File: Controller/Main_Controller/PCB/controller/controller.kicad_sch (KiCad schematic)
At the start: 118 parts, among them Q1 S9013, U1 NUCLEO144-F429ZI, U2 Joystick, U3 Joystick, U4 ZSR330GTA, U5 ZLDO1117G50TA

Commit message: Add Reverse polarity protection
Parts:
- removed D4, D5: B5817W-5819W, Diode_SMD:D_SOD-123, symbol Diode:1N5817
- added D?: D, symbol Device:D
- added Q?: Q_PMOS_DGS, symbol Device:Q_PMOS_DGS
- added R?: R, symbol Device:R
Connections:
- net Earth: now also R?.2
- net VIN: now also Q?.1 (D); no longer PWR_SW1.2 (B)
- new net: D?.2 (A), Q?.2 (G), R?.1
- new net: D?.1 (K), PWR_SW1.2 (B), Q?.3 (S)
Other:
- moved on the sheet: C?, D?, M?, PWR_SW1, Q?, R?, U1

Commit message: uPDATE sCHEMATIC - ADD MOST BUTTONS
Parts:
- removed BTN, D_SEL, RESET?: SW_SPST, Button_Switch_SMD:SW_Push_1P1T_NO_6x6mm_H9.5mm, symbol Switch:SW_SPST
- removed C? (x7): 100nF, Capacitor_SMD:C_0603_1608Metric, symbol Device:C
- removed D? (x7): D, symbol Device:D
- removed R? (x14): 47K, Resistor_SMD:R_0603_1608Metric, symbol Device:R
- removed R?: 2K2, Resistor_SMD:R_0603_1608Metric, symbol Device:R
- removed R?: 10K, Resistor_SMD:R_0603_1608Metric, symbol Device:R
- removed U? (x14): 74HC7014, Package_SO:SOIC-14_3.9x8.7mm_P1.27mm, symbol 74xx:74HC7014
- added ASCEND, DESCEND, LIGHTS, MOTOR_ENGAGE, REV_BRAKE, REV_BRAKE?: SW_SPDT, symbol Switch:SW_SPDT
- added C? (x16): 100nF, Capacitor_SMD:C_0603_1608Metric, symbol Device:C
- added D? (x16): D, symbol Device:D
- added D_BACK, D_SELECT, KILL_SWITCH: SW_SPST, Button_Switch_SMD:SW_Push_1P1T_NO_6x6mm_H9.5mm, symbol Switch:SW_SPST
- added J?: Conn_01x10, symbol Connector_Generic:Conn_01x10
- added R? (x32): 47K, Resistor_SMD:R_0603_1608Metric, symbol Device:R
- added R? (x2): 4K7, Resistor_SMD:R_0603_1608Metric, symbol Device:R
- added U? (x21): 74HC7014, Package_SO:SOIC-14_3.9x8.7mm_P1.27mm, symbol 74xx:74HC7014
- gave numbers to parts that had none: 1
- renumbered R2 to R?, R1 to R?, RESET1 to RESET
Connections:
- net RESET_1 is gone; now on net RESET: A1.3 (~{RESET}), R3.2
- net +3V3: now also U1.16 (+3V3), R?.1, R?.1, U?.14 (VCC), U?.14 (VCC), U?.14 (VCC)
- net +5V: now also U1.18 (+5V), R?.2, R?.2, R?.2, R?.2, R?.2, R?.2, R?.2, R?.2, R?.2, R?.2, R?.2, R?.2, R?.2, R?.2, R?.2, R?.2
- net D_DOWN: now also A1.20 (A1), U?.4
- net D_LEFT: now also A1.21 (A2), U?.6
- net D_RIGHT: now also A1.22 (A3), U?.8
- net D_UP: now also A1.19 (A0), U?.2
- net Earth: now also U1.111 (GND), U1.126 (GND), U1.135 (GND), U1.143 (GND), U1.144 (GND), U1.19 (GND), U1.20 (GND), U1.22 (GND), U1.49 (GND), U1.60 (GND), U1.71 (GND), U1.72 (GND), U1.8 (GND), U1.81 (GND), U1.92 (GND), ASCEND.2 (B), C?.1, C?.1, C?.1, C?.1, C?.1, C?.1, C?.1, C?.1, C?.1, C?.1, C?.1, C?.1, C?.1, C?.1, C?.1, C?.1, DESCEND.2 (B), D_BACK.1 (A), D_SELECT.1 (A), J?.2 (Pin_2), J?.5 (Pin_5), J?.8 (Pin_8), KILL_SWITCH.1 (A), LIGHTS.2 (B), MOTOR_ENGAGE.2 (B), REV_BRAKE.2 (B), REV_BRAKE?.2 (B), U?.7 (GND), U?.7 (GND), U?.7 (GND)
- net LCD_E: now also A1.6 (D3); no longer A1.10 (D7)
- net LCD_R/W: now also A1.9 (D6); no longer A1.11 (D8)
- net LED_1: now also A1.5 (D2); no longer A1.2 (D0/RX)
- net MOTOR_MODE_1: now also U?.2
- net MOTOR_MODE_2: now also U?.4
- net VIN: now also J?.1 (Pin_1)
- net D_SELECT: now reaches A1.25 (A6)
- net D_SELECT: now also U?.10
- net D_BACK: now reaches A1.26 (A7)
- net D_BACK: now also U?.12
- net SDA_1: now reaches A1.7 (D4)
- net SDA_1: now also J?.3 (Pin_3), R?.2
- net CLK_1: now reaches A1.8 (D5)
- net CLK_1: now also R?.2
- net at MOTOR_MODE.3 (C): now also D?.2 (A), R?.1, R?.2
- net at D_RIGHT.2 (B): now also D?.2 (A), R?.1, R?.2
- net at MOTOR_MODE.1 (A): now also D?.2 (A), R?.1, R?.2
- net at D_LEFT.2 (B): now also D?.2 (A), R?.1, R?.2
- net RESET: now reaches U1.14 (~{RST})
- net at C?.2, D?.1 (K), R?.1: now also U?.1
- net at D_DOWN.2 (B): now also D?.2 (A), R?.1, R?.2
- new net: C?.2, D?.1 (K), R?.1, U?.13 (x2)
- new net: D?.2 (A), MOTOR_ENGAGE.1 (A), R?.1, R?.2
- new net: C?.2, D?.1 (K), R?.1, U?.3 (x3)
- new net: C?.2, D?.1 (K), R?.1, U?.5 (x3)
- new net: D?.2 (A), R?.1, R?.2, REV_BRAKE?.1 (A)
- new net: C?.2, D?.1 (K), R?.1, U?.1 (x2)
- new net: D?.2 (A), R?.1, R?.2, REV_BRAKE?.3 (C)
- new net: C?.2, D?.1 (K), R?.1, U?.9 (x3)
- new net: D?.2 (A), D_BACK.2 (B), R?.1, R?.2
- new net: D?.2 (A), R?.1, R?.2, REV_BRAKE.3 (C)
- new net: D?.2 (A), R?.1, R?.2, REV_BRAKE.1 (A)
- new net: D?.2 (A), KILL_SWITCH.2 (B), R?.1, R?.2
- new net: C?.2, D?.1 (K), R?.1
- new net: ASCEND.1 (A), D?.2 (A), R?.1, R?.2
- new net: C?.2, D?.1 (K), R?.1, U?.11 (x2)
- new net: D?.2 (A), DESCEND.1 (A), R?.1, R?.2
- new net: D?.2 (A), D_SELECT.2 (B), R?.1, R?.2
- new net: D?.2 (A), LIGHTS.1 (A), R?.1, R?.2
- new net ASCEND: U?.8
- new net BRAKE_MODE: U?.2
- new net DESCEND: U?.10
- new net DET_IN: J?.9 (Pin_9)
- new net DET_OUT: J?.10 (Pin_10)
- new net KILL_SWITCH: U?.6
- new net MOTOR_DENGAGE: U?.8
- new net MOTOR_ENGAGE: U?.12, U?.6
- new net REV_MODE: U?.4
- new net SCK_1: J?.4 (Pin_4)
- new net SCK_2: J?.7 (Pin_7)
- new net SDA_2: J?.6 (Pin_6)
- no-connect marks 12 -> 31
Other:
- note added: "BUZZER"
- note added: "CONNECTOR"
- note added: "D-PAD"
- note added: "JOYSTICKS"
- note added: "LCD"
- note added: "NUCLEO-F429ZI"
- note added: "NUCLEO-L432KC"
- note added: "POWER"
- note added: "VIBRATION MOTOR"
- company: Luke W -> Sirmon Industries, Luke Waller, Noah Harvey, Jack Pendlebury, Daniel Cole 
- title: Project ORCA Controller -> HEVCS Controller
- moved on the sheet: A1, BZ?, C1, C2, C3, C4, C?, D1, D2, D3, D?, DS?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

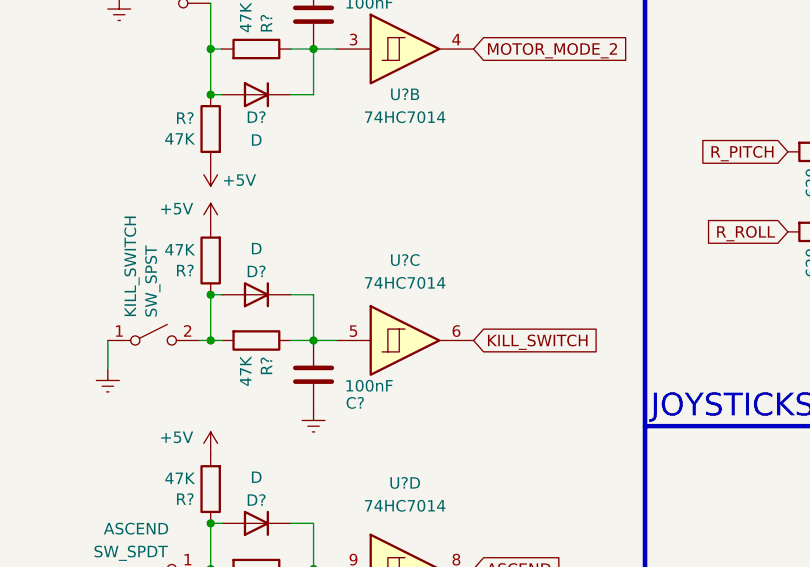
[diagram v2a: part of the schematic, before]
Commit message: verified schmitt trigger functionality
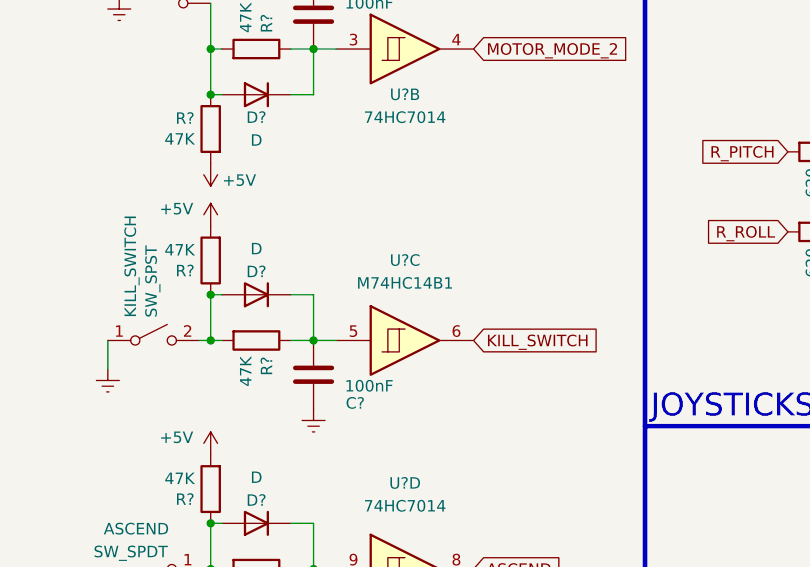
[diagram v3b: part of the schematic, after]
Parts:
- U?: value 74HC7014 -> M74HC14B1
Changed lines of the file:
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@@
     (in_bom yes) (on_board yes) (fields_autoplaced)
     (property "Reference" "U?" (id 0) (at 233.68 68.58 0))
-    (property "Value" "74HC7014" (id 1) (at 233.68 71.12 0))
+    (property "Value" "M74HC14B1" (id 1) (at 233.68 71.12 0))
     (property "Footprint" "Package_SO:SOIC-14_3.9x8.7mm_P1.27mm" (id 2) (at 233.68 77.47 0)
       (effects (font (size 1.27 1.27)) hide)
@@
     )
     (path "/afe26da9-bfe2-4ef8-993f-8605163ec6eb"
-      (reference "U?") (unit 3) (value "74HC7014") (footprint "Package_SO:SOIC-14_3.9x8.7mm_P1.27mm")
+      (reference "U?") (unit 3) (value "M74HC14B1") (footprint "Package_SO:SOIC-14_3.9x8.7mm_P1.27mm")
     )
     (path "/e7f76d38-76ff-4182-add0-0aac4e530149"

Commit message: started adding solder bridges
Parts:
- removed C?: 100nF, Capacitor_SMD:C_0603_1608Metric, symbol Device:C
- removed D?: D, symbol Device:D
- removed MOTOR_ENGAGE: SW_SPDT, symbol Switch:SW_SPDT
- removed R? (x2): 47K, Resistor_SMD:R_0603_1608Metric, symbol Device:R
- removed U?: 74HC7014, Package_SO:SOIC-14_3.9x8.7mm_P1.27mm, symbol 74xx:74HC7014
- added C? (x3): 100nF, Capacitor_SMD:C_0603_1608Metric, symbol Device:C
- added JP? (x7): SolderJumper_3_Open, symbol Jumper:SolderJumper_3_Open
- added U?: 74HC7014, Package_SO:SOIC-14_3.9x8.7mm_P1.27mm, symbol 74xx:74HC7014
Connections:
- net +3V3: now also C?.1, C?.1, C?.1, JP?.1 (A), JP?.1 (A), JP?.1 (A), JP?.1 (A), JP?.1 (A), JP?.1 (A), JP?.1 (A)
- net D_BACK: now also JP?.2 (C)
- net D_DOWN: now also JP?.2 (C)
- net D_LEFT: now also JP?.2 (C)
- net D_RIGHT: now also JP?.2 (C)
- net D_SELECT: now also JP?.2 (C)
- net D_UP: now also JP?.2 (C)
- net Earth: now also C?.2, C?.2, C?.2, JP?.3 (B), JP?.3 (B), JP?.3 (B), JP?.3 (B), JP?.3 (B), JP?.3 (B), JP?.3 (B); no longer C?.1
- net LIGHTS: now also U?.12
- net at C?.2, D?.1 (K), R?.1: now also U?.13
- no-connect marks 31 -> 30
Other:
- moved on the sheet: C?, D1, D?, D_BACK, D_DOWN, D_LEFT, D_RIGHT, D_SELECT, D_UP, J?, LIGHTS, Q1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
